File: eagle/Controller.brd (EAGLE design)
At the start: 101.6 x 72.4 mm, 41 parts, among them Q1 IRF530N, Q2 IRF530N, Q3 IRF530N, Q4 IRF530N, Q5 IRF530N, Q6 IRF530N, U1 BC337

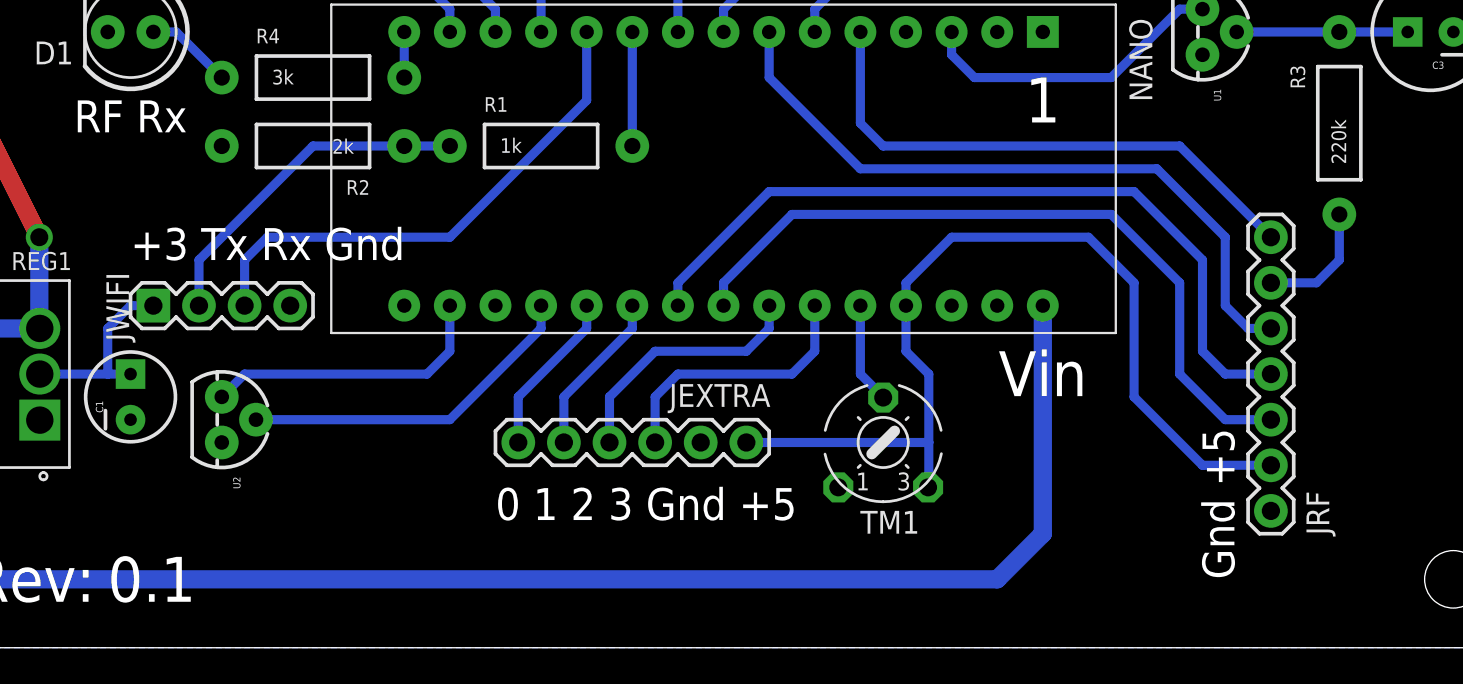
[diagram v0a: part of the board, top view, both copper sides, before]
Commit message: Change reset circuit to work with lower Arduino resistor values
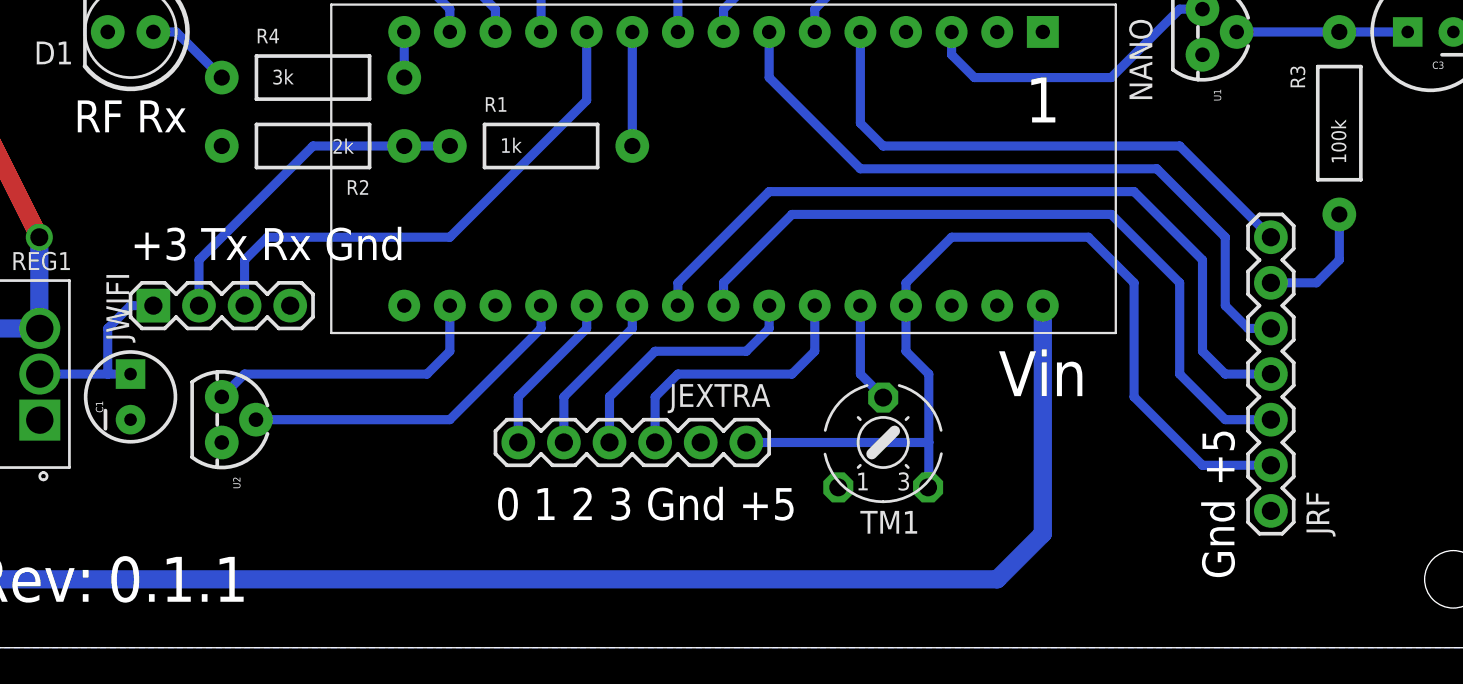
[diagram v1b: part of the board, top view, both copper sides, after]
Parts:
- C3: value 100uF -> 220uF
- R3: value 220k -> 100k
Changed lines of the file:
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@@
 </plain>
 <attributes>
-<attribute name="CREVISION" value="0.1"/>
+<attribute name="CREVISION" value="0.1.1"/>
 </attributes>
 <variantdefs>
@@
 <attribute name="VALUE" x="24.13" y="15.875" size="1.27" layer="27"/>
 </element>
-<element name="R3" library="SparkFun-Passives" package="AXIAL-0.4" value="220k" x="91.44" y="29.21" smashed="yes" rot="R90">
+<element name="R3" library="SparkFun-Passives" package="AXIAL-0.4" value="100k" x="91.44" y="29.21" smashed="yes" rot="R90">
 <attribute name="NAME" x="89.535" y="31.115" size="0.8128" layer="25" font="vector" ratio="15" rot="R90"/>
 <attribute name="VALUE" x="91.821" y="26.924" size="0.8128" layer="21" font="vector" ratio="15" rot="R90"/>
 </element>
-<element name="C3" library="SparkFun-Capacitors" package="CPOL-RADIAL-100UF-25V" value="100uF" x="96.52" y="34.29" rot="R180">
+<element name="C3" library="SparkFun-Capacitors" package="CPOL-RADIAL-100UF-25V" value="220uF" x="96.52" y="34.29" rot="R180">
 <attribute name="PROD_ID" value="CAP-08439" x="96.52" y="34.29" size="1.778" layer="27" rot="R180" display="off"/>
 </element>
